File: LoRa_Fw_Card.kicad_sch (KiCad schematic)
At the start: 11 parts, among them P1 USB_C_Plug_USB2.0, U1 AP2112K-3.3

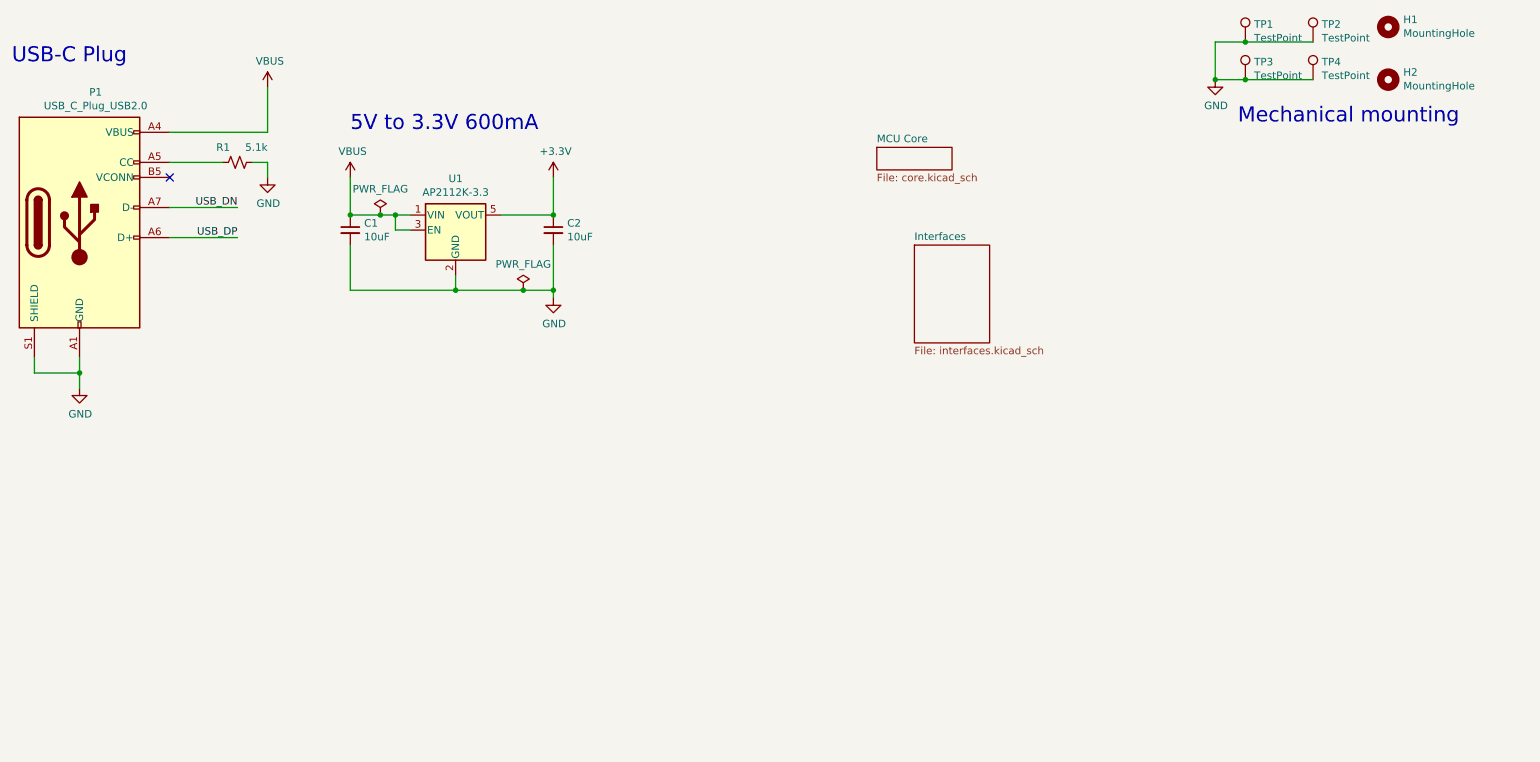
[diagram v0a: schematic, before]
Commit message: Add partial RF and Memory wiring and placement
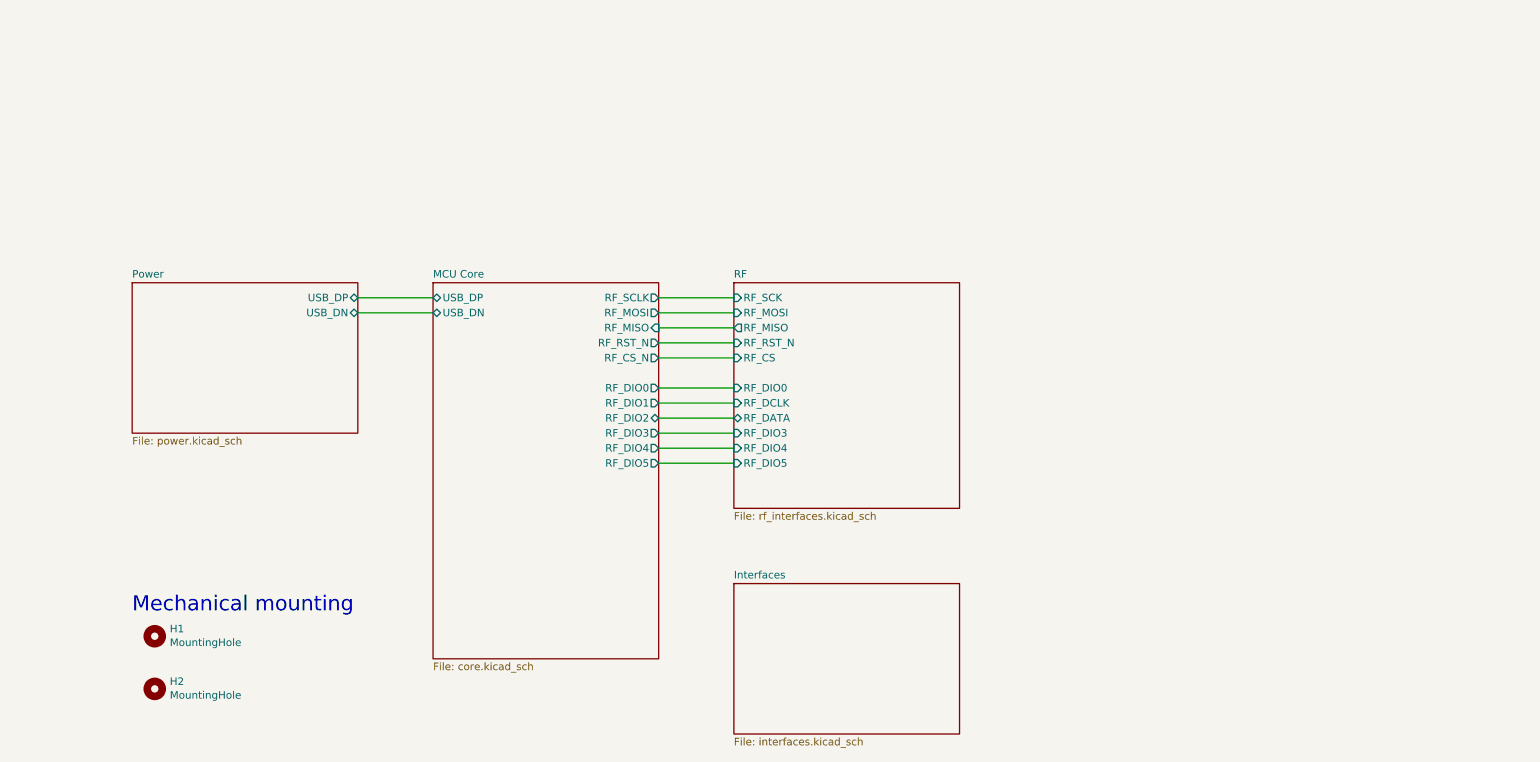
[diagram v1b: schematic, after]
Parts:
- removed C1, C2: 10uF, Capacitor_SMD:C_0805_2012Metric, symbol Device:C_Small
- removed P1: USB_C_Plug_USB2.0, Expansion_Card:USB_C_Plug_Molex_105444, symbol Connector:USB_C_Plug_USB2.0
- removed R1: 5.1k, Resistor_SMD:R_0603_1608Metric, symbol Device:R_Small_US
- removed TP1, TP2, TP3, TP4: TestPoint, TestPoint:TestPoint_Pad_1.5x1.5mm, symbol Connector:TestPoint
- removed U1: AP2112K-3.3, Package_TO_SOT_SMD:SOT-23-5, symbol Regulator_Linear:AP2112K-3.3
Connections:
- no-connect marks 1 -> 0
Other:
- added sheet Power (power.kicad_sch)
- added sheet RF (rf_interfaces.kicad_sch)
- sheet MCU Core ports: added RF_CS_N, RF_DIO0, RF_DIO1, RF_DIO2, RF_DIO3, RF_DIO4, RF_DIO5, RF_MISO, RF_MOSI, RF_RST_N, RF_SCLK, USB_DN, USB_DP; removed none
- note removed: "5V to 3.3V 600mA"
- note removed: "USB-C Plug"
- title: Expansion Card Template -> LoRa Expansion Card for Frame.Work Laptop
- moved on the sheet: H1, H2
